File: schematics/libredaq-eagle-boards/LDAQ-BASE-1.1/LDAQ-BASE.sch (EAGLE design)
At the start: 90 parts, among them J1 PJ-102A, J2 3221-10-0100-00, T1 FDN340P, U1 ATSAM3U1CB, U2 LM3671MF-3.3, U3 TS30012-M050QFNR, U4 ISL3175, U5 LMV321, U6 TXB0108PWR, Y1 12M

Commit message: Update connectors in BASE
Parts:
- C11, C23, C28, C29, C30, C31, C32, C33: device SparkFun-Capacitors:CAP0805 -> SparkFun-Capacitors:CAP-0805
- C12, C13, C21, C22: device SparkFun-Capacitors:CAP1206 -> SparkFun-Capacitors:CAP-1206
- JP1: value SCREWTERMINAL-3.5MM-9 -> 39357-0009; device libredaq-comps:SCREWTERMINAL-3.5MM-9 -> SamacSys_Parts:39357-0009
- JP2: value SCREWTERMINAL-3.5MM-6 -> 1984659; device libredaq-comps:SCREWTERMINAL-3.5MM-6 -> SamacSys_Parts:1984659
- JP3: value SCREWTERMINAL-3.5MM-5 -> 1984646; device libredaq-comps:SCREWTERMINAL-3.5MM-5 -> SamacSys_Parts:1984646
- R1, R2: value 39R 1% -> (none)
- R3: value 6K8 1% -> (none)
- R5: value 120R -> (none)
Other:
- note added: "Amphenol ICC / FCI 10018783-10201TLF"
- moved on the sheet: JP1, JP2, JP3
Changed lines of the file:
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@@
 <layer number="115" name="ReferenceISLANDS" color="7" fill="1" visible="no" active="no"/>
 <layer number="116" name="Patch_BOT" color="9" fill="4" visible="yes" active="yes"/>
+<layer number="117" name="PM_Ref" color="7" fill="1" visible="no" active="no"/>
 <layer number="118" name="Rect_Pads" color="7" fill="1" visible="yes" active="yes"/>
+<layer number="119" name="PF_Ref" color="7" fill="1" visible="no" active="no"/>
+<layer number="120" name="WFL_Ref" color="7" fill="1" visible="no" active="no"/>
 <layer number="121" name="_tsilk" color="7" fill="1" visible="yes" active="yes"/>
 <layer number="122" name="_bsilk" color="7" fill="1" visible="yes" active="yes"/>
@@
 <part name="GND5" library="SparkFun-Aesthetics" deviceset="GND" device=""/>
 <part name="GND6" library="SparkFun-Aesthetics" deviceset="GND" device=""/>
-<part name="R1" library="SparkFun-Resistors" deviceset="RESISTOR" device="1206" value="39R 1%"/>
-<part name="R2" library="SparkFun-Resistors" deviceset="RESISTOR" device="0603" value="39R 1%"/>
-<part name="R3" library="SparkFun-Resistors" deviceset="RESISTOR" device="0603" value="6K8 1%"/>
+<part name="R1" library="SparkFun-Resistors" deviceset="RESISTOR" device="1206" value=" "/>
+<part name="R2" library="SparkFun-Resistors" deviceset="RESISTOR" device="0603" value=" "/>
+<part name="R3" library="SparkFun-Resistors" deviceset="RESISTOR" device="0603" value=" "/>
 <part name="C3" library="SparkFun-Capacitors" deviceset="10PF-50V-5%(0603)" device="" value="10pF"/>
 <part name="Y1" library="SparkFun-FreqCtrl" deviceset="CRYSTAL" device="5X3" value="12M"/>
@@
 <part name="GND32" library="SparkFun-Aesthetics" deviceset="GND" device=""/>
 <part name="GND17" library="SparkFun-Aesthetics" deviceset="GND" device=""/>
-<part name="R5" library="SparkFun-Resistors" deviceset="RESISTOR" device="0603" value="120R"/>
+<part name="R5" library="SparkFun-Resistors" deviceset="RESISTOR" device="0603" value=" "/>
 <part name="GND33" library="SparkFun-Aesthetics" deviceset="GND" device=""/>
 <part name="SJ1" library="libredaq-comps" deviceset="JUMPER-PTH-2OF3-P0.1" device=""/>
@@
 <part name="C14" library="SparkFun-Capacitors" deviceset="10UF-6.3V-20%(0603)" device="" value="10uF"/>
 <part name="GND16" library="SparkFun-Aesthetics" deviceset="GND" device=""/>
-<part name="JP1" library="libredaq-comps" deviceset="SCREWTERMINAL-3.5MM-9" device="" value="SCREWTERMINAL-3.5MM-9"/>
+<part name="JP1" library="SamacSys_Parts" deviceset="39357-0009" device="" value="39357-0009"/>
 <part name="GND19" library="SparkFun-Aesthetics" deviceset="GND" device=""/>
 <part name="R12" library="SparkFun-Resistors" deviceset="RESISTOR-ARRAY" device="0603-ARV" value="100K"/>
@@
 <part name="R9" library="SparkFun-Resistors" deviceset="100KOHM-1/10W-1%(0603)" device="" value="100k"/>
 <part name="GND36" library="supply1" deviceset="GND" device=""/>
-<part name="C12" library="SparkFun-Capacitors" deviceset="CAP" device="1206" value="22uF"/>
-<part name="C13" library="SparkFun-Capacitors" deviceset="CAP" device="1206" value="22uF"/>
+<part name="C12" library="SparkFun-Capacitors" deviceset="CAP" device="-1206" value="22uF"/>
+<part name="C13" library="SparkFun-Capacitors" deviceset="CAP" device="-1206" value="22uF"/>
 <part name="GND38" library="supply1" deviceset="GND" device=""/>
-<part name="C21" library="SparkFun-Capacitors" deviceset="CAP" device="1206" value="10uF"/>
-<part name="C22" library="SparkFun-Capacitors" deviceset="CAP" device="1206" value="10uF"/>
+<part name="C21" library="SparkFun-Capacitors" deviceset="CAP" device="-1206" value="10uF"/>
+<part name="C22" library="SparkFun-Capacitors" deviceset="CAP" device="-1206" value="10uF"/>
 <part name="GND39" library="supply1" deviceset="GND" device=""/>
 <part name="GND45" library="supply1" deviceset="GND" device=""/>
@@
 <part name="SUPPLY21" library="SparkFun-Aesthetics" deviceset="3.3V" device=""/>
 <part name="SUPPLY25" library="SparkFun-Aesthetics" deviceset="3.3V" device=""/>
-<part name="C11" library="SparkFun-Capacitors" deviceset="CAP" device="0805" value="1uF"/>
+<part name="C11" library="SparkFun-Capacitors" deviceset="CAP" device="-0805" value="1uF"/>
 <part name="GND35" library="SparkFun-Aesthetics" deviceset="GND" device=""/>
 <part name="P+4" library="supply1" deviceset="+5V" device=""/>
-<part name="C23" library="SparkFun-Capacitors" deviceset="CAP" device="0805" value="1uF"/>
+<part name="C23" library="SparkFun-Capacitors" deviceset="CAP" device="-0805" value="1uF"/>
 <part name="GND47" library="SparkFun-Aesthetics" deviceset="GND" device=""/>
 <part name="SUPPLY18" library="SparkFun-Aesthetics" deviceset="3.3V" device=""/>
-<part name="C28" library="SparkFun-Capacitors" deviceset="CAP" device="0805" value="1uF"/>
+<part name="C28" library="SparkFun-Capacitors" deviceset="CAP" device="-0805" value="1uF"/>
 <part name="GND48" library="SparkFun-Aesthetics" deviceset="GND" device=""/>
 <part name="P+5" library="supply1" deviceset="+5V" device=""/>
-<part name="C29" library="SparkFun-Capacitors" deviceset="CAP" device="0805" value="1uF"/>
+<part name="C29" library="SparkFun-Capacitors" deviceset="CAP" device="-0805" value="1uF"/>
 <part name="GND49" library="SparkFun-Aesthetics" deviceset="GND" device=""/>
 <part name="SUPPLY20" library="SparkFun-Aesthetics" deviceset="3.3V" device=""/>
-<part name="C30" library="SparkFun-Capacitors" deviceset="CAP" device="0805" value="1uF"/>
+<part name="C30" library="SparkFun-Capacitors" deviceset="CAP" device="-0805" value="1uF"/>
 <part name="GND50" library="SparkFun-Aesthetics" deviceset="GND" device=""/>
 <part name="P+6" library="supply1" deviceset="+5V" device=""/>
-<part name="C31" library="SparkFun-Capacitors" deviceset="CAP" device="0805" value="1uF"/>
+<part name="C31" library="SparkFun-Capacitors" deviceset="CAP" device="-0805" value="1uF"/>
 <part name="GND51" library="SparkFun-Aesthetics" deviceset="GND" device=""/>
 <part name="SUPPLY24" library="SparkFun-Aesthetics" deviceset="3.3V" device=""/>
-<part name="C32" library="SparkFun-Capacitors" deviceset="CAP" device="0805" value="1uF"/>
+<part name="C32" library="SparkFun-Capacitors" deviceset="CAP" device="-0805" value="1uF"/>
 <part name="GND52" library="SparkFun-Aesthetics" deviceset="GND" device=""/>
 <part name="P+7" library="supply1" deviceset="+5V" device=""/>
-<part name="C33" library="SparkFun-Capacitors" deviceset="CAP" device="0805" value="1uF"/>
+<part name="C33" library="SparkFun-Capacitors" deviceset="CAP" device="-0805" value="1uF"/>
 <part name="GND53" library="SparkFun-Aesthetics" deviceset="GND" device=""/>
-<part name="JP2" library="libredaq-comps" deviceset="SCREWTERMINAL-3.5MM-6" device=""/>
+<part name="JP2" library="SamacSys_Parts" deviceset="1984659" device=""/>
 <part name="GND54" library="SparkFun-Aesthetics" deviceset="GND" device=""/>
-<part name="JP3" library="libredaq-comps" deviceset="SCREWTERMINAL-3.5MM-5" device=""/>
+<part name="JP3" library="SamacSys_Parts" deviceset="1984646" device=""/>
 <part name="GND55" library="SparkFun-Aesthetics" deviceset="GND" device=""/>
 <part name="SUPPLY26" library="SparkFun-Aesthetics" deviceset="3.3V" device=""/>
@@
 <text x="25.4" y="289.56" size="1.778" layer="91">JTAG connector: 10 pins IDC
 1175-1733-ND</text>
+<text x="381" y="406.4" size="1.778" layer="91">Amphenol ICC / FCI
+10018783-10201TLF</text>
 </plain>
 <instances>
@@
 <attribute name="VALUE" x="297.18" y="251.46" size="1.778" layer="96"/>
 </instance>
-<instance part="JP1" gate="G$1" x="281.94" y="160.02" smashed="yes" rot="R180">
-<attribute name="NAME" x="284.48" y="154.178" size="1.778" layer="95" rot="R180"/>
+<instance part="JP1" gate="G$1" x="274.32" y="157.48" smashed="yes" rot="MR180">
+<attribute name="NAME" x="271.78" y="151.638" size="1.778" layer="95" rot="MR180"/>
 </instance>
 <instance part="GND19" gate="1" x="157.48" y="292.1" smashed="yes" rot="R270">
@@
 <attribute name="VALUE" x="452.12" y="381" size="1.778" layer="96"/>
 </instance>
-<instance part="JP2" gate="G$1" x="312.42" y="403.86" smashed="yes" rot="R180">
-<attribute name="NAME" x="314.96" y="395.478" size="1.778" layer="95" rot="R180"/>
+<instance part="JP2" gate="G$1" x="304.8" y="398.78" smashed="yes" rot="MR180">
+<attribute name="NAME" x="309.88" y="417.068" size="1.778" layer="95" rot="MR180"/>
 </instance>
 <instance part="GND54" gate="1" x="304.8" y="388.62" smashed="yes" rot="MR0">
 <attribute name="VALUE" x="307.34" y="386.08" size="1.778" layer="96" rot="MR0"/>
 </instance>
-<instance part="JP3" gate="G$1" x="25.4" y="350.52" smashed="yes" rot="MR180">
-<attribute name="NAME" x="22.86" y="344.678" size="1.778" layer="95" rot="MR180"/>
+<instance part="JP3" gate="G$1" x="33.02" y="347.98" smashed="yes" rot="R180">
+<attribute name="NAME" x="35.56" y="342.138" size="1.778" layer="95" rot="R180"/>
 </instance>
 <instance part="GND55" gate="1" x="38.1" y="363.22" smashed="yes" rot="R180">

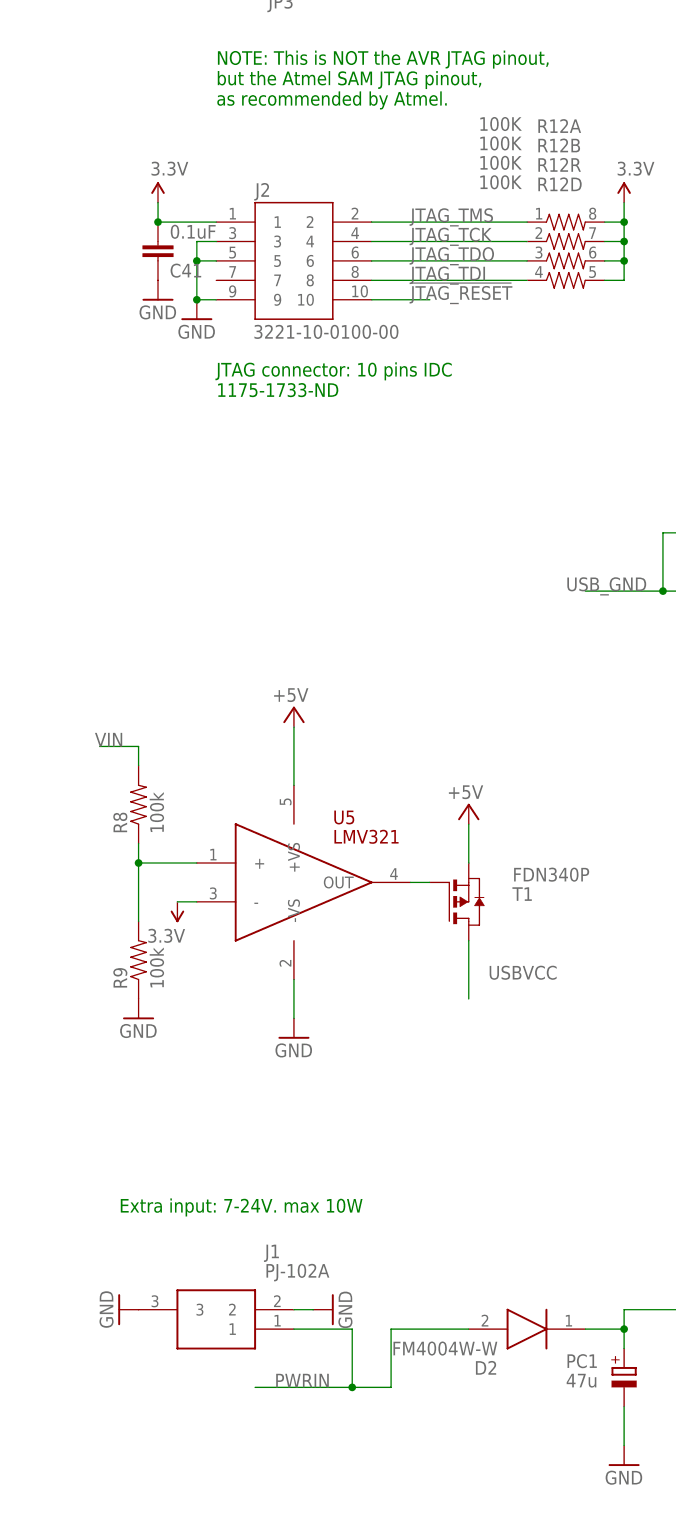
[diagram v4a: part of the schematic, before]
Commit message: optimized board size
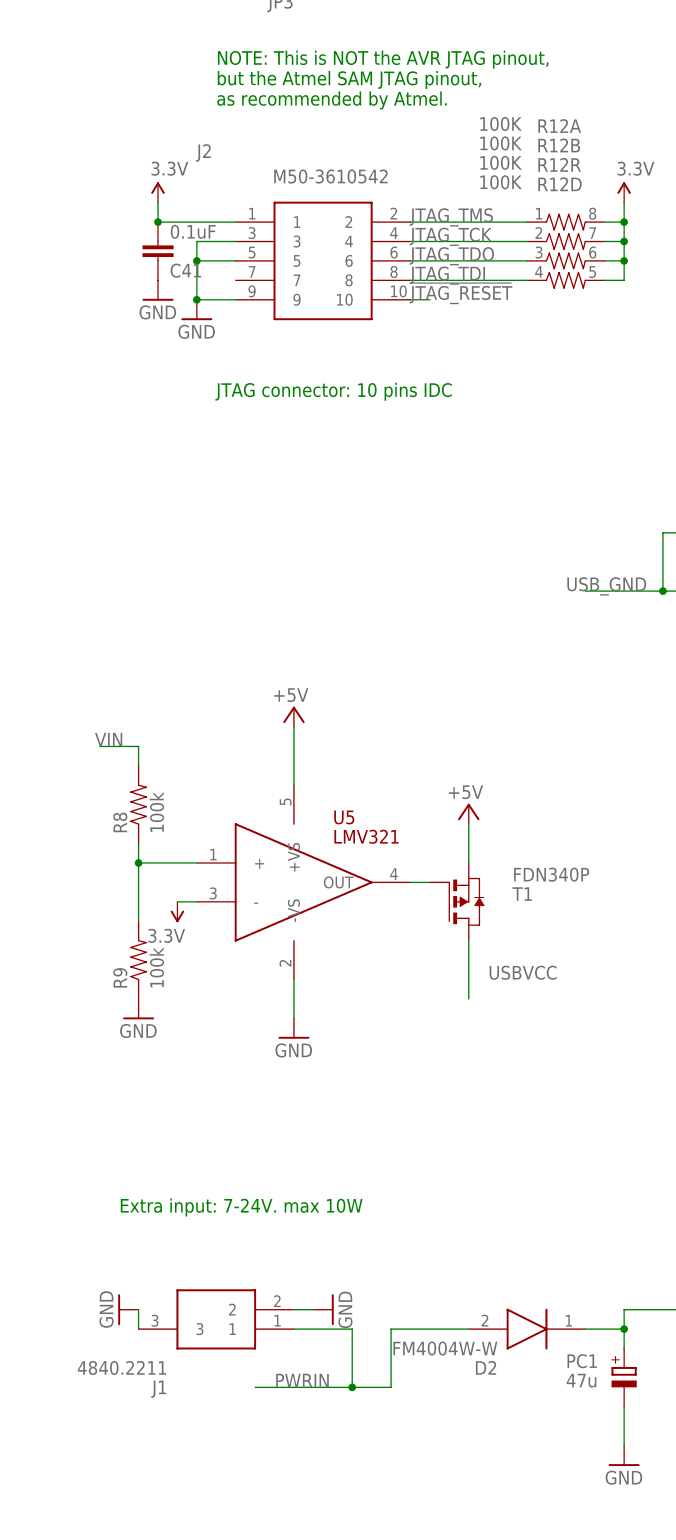
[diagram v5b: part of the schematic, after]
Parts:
- J1: value PJ-102A -> 4840.2211; device PJ-102A:PJ-102A -> SamacSys_Parts:4840.2211
- J2: value 3221-10-0100-00 -> M50-3610542; device 3221-10-0100-00:3221-10-0100-00 -> SamacSys_Parts:M50-3610542
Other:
- note added: "JTAG connector: 10 pins IDC"
- note removed: "JTAG connector: 10 pins IDC 1175-1733-ND"
- moved on the sheet: J1, J2
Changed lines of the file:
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@@
 <part name="C38" library="SparkFun-Capacitors" deviceset="0.1UF-25V(+80/-20%)(0603)" device="" value="4.7uF"/>
 <part name="U3" library="TS30012-M050QFNR" deviceset="TS30012-M050QFNR" device=""/>
-<part name="J1" library="PJ-102A" deviceset="PJ-102A" device=""/>
+<part name="J1" library="SamacSys_Parts" deviceset="4840.2211" device=""/>
 <part name="GND37" library="supply1" deviceset="GND" device=""/>
 <part name="D2" library="FM4004W-W" deviceset="FM4004W-W" device=""/>
@@
 <part name="GND60" library="SparkFun-Aesthetics" deviceset="GND" device=""/>
 <part name="GND61" library="SparkFun-Aesthetics" deviceset="GND" device=""/>
-<part name="J2" library="3221-10-0100-00" deviceset="3221-10-0100-00" device=""/>
+<part name="J2" library="SamacSys_Parts" deviceset="M50-3610542" device=""/>
 <part name="C41" library="SparkFun-Capacitors" deviceset="0.1UF-25V(+80/-20%)(0603)" device="" value="0.1uF"/>
 <part name="GND62" library="SparkFun-Aesthetics" deviceset="GND" device=""/>
@@
 Put this capacitor CLOSE to the chip</text>
 <text x="25.4" y="289.56" size="1.778" layer="91">JTAG connector: 10 pins IDC
-1175-1733-ND</text>
+</text>
 <text x="381" y="406.4" size="1.778" layer="91">Amphenol ICC / FCI
 10018783-10201TLF</text>
@@
 <attribute name="VALUE" x="173.99" y="96.52" size="1.778" layer="96" align="center-left"/>
 </instance>
-<instance part="J1" gate="G$1" x="15.24" y="170.18" smashed="yes">
-<attribute name="NAME" x="31.75" y="177.8" size="1.778" layer="95" align="center-left"/>
-<attribute name="VALUE" x="31.75" y="175.26" size="1.778" layer="96" align="center-left"/>
+<instance part="J1" gate="G$1" x="35.56" y="167.64" smashed="yes" rot="R180">
+<attribute name="NAME" x="19.05" y="160.02" size="1.778" layer="95" rot="R180" align="center-left"/>
+<attribute name="VALUE" x="19.05" y="162.56" size="1.778" layer="96" rot="R180" align="center-left"/>
 </instance>
 <instance part="GND37" gate="1" x="12.7" y="170.18" smashed="yes" rot="R270">
@@
 <attribute name="VALUE" x="160.02" y="193.04" size="1.778" layer="96" rot="R180"/>
 </instance>
-<instance part="J2" gate="G$1" x="35.56" y="307.34" smashed="yes">
-<attribute name="NAME" x="30.47961875" y="315.72263125" size="1.77813125" layer="95"/>
-<attribute name="VALUE" x="30.22183125" y="298.95145" size="1.779390625" layer="96" rot="MR180"/>
+<instance part="J2" gate="G$1" x="27.94" y="312.42" smashed="yes">
+<attribute name="NAME" x="22.85961875" y="320.80263125" size="1.77813125" layer="95"/>
+<attribute name="VALUE" x="32.76183125" y="319.27145" size="1.779390625" layer="96" rot="MR180"/>
 </instance>
 <instance part="C41" gate="G$1" x="17.78" y="309.88" smashed="yes" rot="MR180">
@@
 </segment>
 <segment>
-<pinref part="J1" gate="G$1" pin="2"/>
-<wire x1="35.56" y1="170.18" x2="38.1" y2="170.18" width="0.1524" layer="91"/>
-<pinref part="GND14" gate="1" pin="GND"/>
-</segment>
-<segment>
-<pinref part="J1" gate="G$1" pin="3"/>
-<pinref part="GND37" gate="1" pin="GND"/>
-</segment>
-<segment>
 <pinref part="U6" gate="G$1" pin="GND"/>
 <pinref part="GND56" gate="1" pin="GND"/>
@@
 <segment>
 <pinref part="J2" gate="G$1" pin="5"/>
-<wire x1="25.4" y1="307.34" x2="22.86" y2="307.34" width="0.1524" layer="91"/>
+<wire x1="27.94" y1="307.34" x2="22.86" y2="307.34" width="0.1524" layer="91"/>
 <wire x1="22.86" y1="307.34" x2="22.86" y2="302.26" width="0.1524" layer="91"/>
 <pinref part="J2" gate="G$1" pin="3"/>
-<wire x1="25.4" y1="309.88" x2="22.86" y2="309.88" width="0.1524" layer="91"/>
+<wire x1="27.94" y1="309.88" x2="22.86" y2="309.88" width="0.1524" layer="91"/>
 <wire x1="22.86" y1="309.88" x2="22.86" y2="307.34" width="0.1524" layer="91"/>
 <junction x="22.86" y="307.34"/>
 <pinref part="GND63" gate="1" pin="GND"/>
 <pinref part="J2" gate="G$1" pin="9"/>
-<wire x1="25.4" y1="302.26" x2="22.86" y2="302.26" width="0.1524" layer="91"/>
+<wire x1="27.94" y1="302.26" x2="22.86" y2="302.26" width="0.1524" layer="91"/>
 <junction x="22.86" y="302.26"/>
+</segment>
+<segment>
+<pinref part="GND37" gate="1" pin="GND"/>
+<pinref part="J1" gate="G$1" pin="3"/>
+<wire x1="15.24" y1="170.18" x2="15.24" y2="167.64" width="0.1524" layer="91"/>
+</segment>
+<segment>
+<pinref part="J1" gate="G$1" pin="2"/>
+<pinref part="GND14" gate="1" pin="GND"/>
+<wire x1="35.56" y1="170.18" x2="38.1" y2="170.18" width="0.1524" layer="91"/>
 </segment>
 </net>
@@
 <segment>
 <pinref part="J2" gate="G$1" pin="1"/>
-<wire x1="25.4" y1="312.42" x2="17.78" y2="312.42" width="0.1524" layer="91"/>
+<wire x1="27.94" y1="312.42" x2="17.78" y2="312.42" width="0.1524" layer="91"/>
 <wire x1="17.78" y1="312.42" x2="17.78" y2="314.96" width="0.1524" layer="91"/>
 <pinref part="C41" gate="G$1" pin="2"/>
@@
 <label x="50.8" y="312.42" size="1.778" layer="95"/>
 <pinref part="R12" gate="A" pin="1"/>
-<wire x1="45.72" y1="312.42" x2="66.04" y2="312.42" width="0.1524" layer="91"/>
+<wire x1="50.8" y1="312.42" x2="66.04" y2="312.42" width="0.1524" layer="91"/>
 <pinref part="J2" gate="G$1" pin="2"/>
 </segment>
@@
 <label x="50.8" y="309.88" size="1.778" layer="95"/>
 <pinref part="R12" gate="B" pin="1"/>
-<wire x1="45.72" y1="309.88" x2="66.04" y2="309.88" width="0.1524" layer="91"/>
+<wire x1="50.8" y1="309.88" x2="66.04" y2="309.88" width="0.1524" layer="91"/>
 <pinref part="J2" gate="G$1" pin="4"/>
 </segment>
@@
 <label x="50.8" y="307.34" size="1.778" layer="95"/>
 <pinref part="R12" gate="R" pin="1"/>
-<wire x1="45.72" y1="307.34" x2="66.04" y2="307.34" width="0.1524" layer="91"/>
+<wire x1="50.8" y1="307.34" x2="66.04" y2="307.34" width="0.1524" layer="91"/>
 <pinref part="J2" gate="G$1" pin="6"/>
 </segment>
@@
 <label x="50.8" y="304.8" size="1.778" layer="95"/>
 <pinref part="R12" gate="D" pin="1"/>
-<wire x1="45.72" y1="304.8" x2="66.04" y2="304.8" width="0.1524" layer="91"/>
+<wire x1="50.8" y1="304.8" x2="66.04" y2="304.8" width="0.1524" layer="91"/>
 <pinref part="J2" gate="G$1" pin="8"/>
 </segment>
@@
 <segment>
 <label x="50.8" y="302.26" size="1.778" layer="95"/>
-<wire x1="45.72" y1="302.26" x2="53.34" y2="302.26" width="0.1524" layer="91"/>
+<wire x1="50.8" y1="302.26" x2="53.34" y2="302.26" width="0.1524" layer="91"/>
 <pinref part="J2" gate="G$1" pin="10"/>
 </segment>
@@
 <wire x1="48.26" y1="160.02" x2="48.26" y2="167.64" width="0.1524" layer="91"/>
 <label x="33.02" y="160.02" size="1.778" layer="95"/>
-<pinref part="J1" gate="G$1" pin="1"/>
-<wire x1="35.56" y1="167.64" x2="43.18" y2="167.64" width="0.1524" layer="91"/>
 <wire x1="43.18" y1="167.64" x2="43.18" y2="160.02" width="0.1524" layer="91"/>
 <junction x="43.18" y="160.02"/>
 <pinref part="D2" gate="G$1" pin="A"/>
 <wire x1="48.26" y1="167.64" x2="58.42" y2="167.64" width="0.1524" layer="91"/>
-</segment>
-</net>
+<pinref part="J1" gate="G$1" pin="1"/>
+<wire x1="35.56" y1="167.64" x2="43.18" y2="167.64" width="0.1524" layer="91"/>
+</segment>
+</net>

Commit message: more missing components in circuithub
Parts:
- removed PWR: BLUE, SparkFun-LED:LED-BLUE1206
- added LED3: 150060RS75000, SamacSys_Parts:150060RS75000
- LED1: value RED -> 150060BS75000; device SparkFun-LED:LED-RED1206 -> SamacSys_Parts:150060BS75000
- LED2: value RED -> 150060RS75000; device SparkFun-LED:LED-RED1206 -> SamacSys_Parts:150060RS75000
- R1: value (none) -> CR1206-FX-39R0ELF; device SparkFun-Resistors:RESISTOR1206 -> SamacSys_Parts:CR1206-FX-39R0ELF
- R2: value (none) -> CR1206-FX-39R0ELF; device SparkFun-Resistors:RESISTOR0603 -> SamacSys_Parts:CR1206-FX-39R0ELF
- R3: value (none) -> SFR03EZPF6801; device SparkFun-Resistors:RESISTOR0603 -> SamacSys_Parts:SFR03EZPF6801
- R5: value (none) -> CRCW0603120RFKEAC; device SparkFun-Resistors:RESISTOR0603 -> SamacSys_Parts:CRCW0603120RFKEAC
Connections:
- removed net N$33: PWR.A, R29.2
- new net N$16: LED1.A, R29.2
- net !LED1: now also LED2.K; no longer LED1.C
- net !LED2: now also LED3.K; no longer LED2.C
- net GND: now also LED1.K; no longer PWR.C
- net N$31: now also LED2.A; no longer LED1.A
- net N$32: now also LED3.A; no longer LED2.A
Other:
- moved on the sheet: SJ1
